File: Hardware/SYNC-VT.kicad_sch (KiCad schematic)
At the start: 0 parts

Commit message: 11/17 progress update
finished the board, now just need to add the peripheral
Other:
- added sheet WiFi_BLE (WiFi_BLE.kicad_sch)
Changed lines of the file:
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@@
+	)
+	(sheet
+		(at 228.6 50.8)
+		(size 25.4 25.4)
+		(fields_autoplaced yes)
+		(stroke
+			(width 0.1524)
+			(type solid)
+		)
+		(fill
+			(color 0 0 0 0.0000)
+		)
+		(property "Sheetname" "WiFi_BLE"
+			(at 228.6 50.0884 0)
+			(effects
+				(font
+					(size 1.27 1.27)
+				)
+				(justify left bottom)
+			)
+		)
+		(property "Sheetfile" "WiFi_BLE.kicad_sch"
+			(at 228.6 76.7846 0)
+			(effects
+				(font
+					(size 1.27 1.27)
+				)
+				(justify left top)
+			)
+		)
+		(instances
+			(project "SYNC-VT"
+				(path "/8b98976c-b0e2-4979-aa9a-b6389ce6c189"
+					(page "8")
+				)
+			)
+		)
 	)
 	(sheet

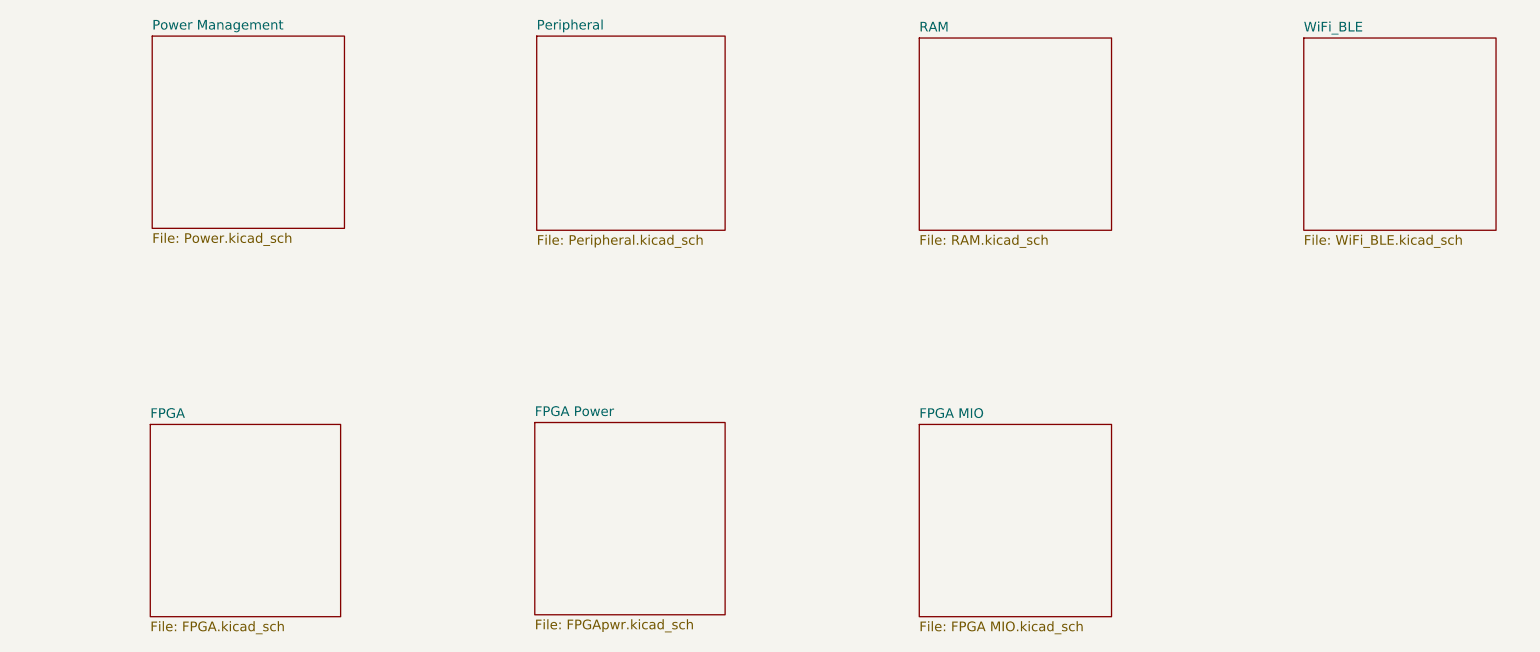
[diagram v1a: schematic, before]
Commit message: 11/19 update
add new header for jtag and fixed a couple of small things
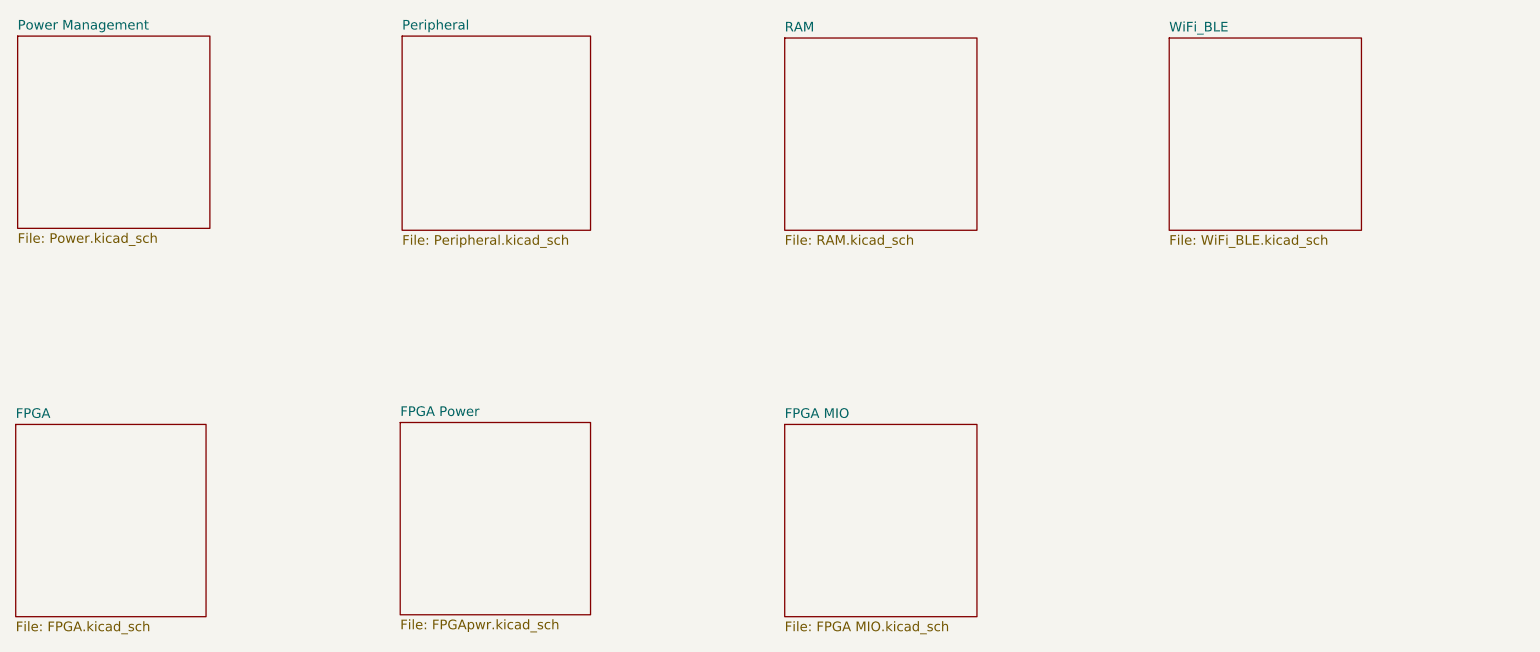
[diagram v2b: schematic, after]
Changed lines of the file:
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@@
 	(paper "A4")
 	(sheet
-		(at 177.8 101.854)
+		(at 160.02 101.854)
 		(size 25.4 25.4)
 		(fields_autoplaced yes)
@@
 		)
 		(property "Sheetname" "FPGA MIO"
-			(at 177.8 101.1424 0)
+			(at 160.02 101.1424 0)
 			(effects
 				(font
@@
 		)
 		(property "Sheetfile" "FPGA MIO.kicad_sch"
-			(at 177.8 127.8386 0)
+			(at 160.02 127.8386 0)
 			(effects
 				(font
@@
 	)
 	(sheet
-		(at 76.454 50.546)
+		(at 58.674 50.546)
 		(size 25.4 25.4)
 		(fields_autoplaced yes)
@@
 		)
 		(property "Sheetname" "Power Management"
-			(at 76.454 49.8344 0)
+			(at 58.674 49.8344 0)
 			(effects
 				(font
@@
 		)
 		(property "Sheetfile" "Power.kicad_sch"
-			(at 76.454 76.5306 0)
+			(at 58.674 76.5306 0)
 			(effects
 				(font
@@
 	)
 	(sheet
-		(at 177.8 50.8)
+		(at 160.02 50.8)
 		(size 25.4 25.4)
 		(fields_autoplaced yes)
@@
 		)
 		(property "Sheetname" "RAM"
-			(at 177.8 50.0884 0)
+			(at 160.02 50.0884 0)
 			(effects
 				(font
@@
 		)
 		(property "Sheetfile" "RAM.kicad_sch"
-			(at 177.8 76.7846 0)
+			(at 160.02 76.7846 0)
 			(effects
 				(font
@@
 	)
 	(sheet
-		(at 228.6 50.8)
+		(at 210.82 50.8)
 		(size 25.4 25.4)
 		(fields_autoplaced yes)
@@
 		)
 		(property "Sheetname" "WiFi_BLE"
-			(at 228.6 50.0884 0)
+			(at 210.82 50.0884 0)
 			(effects
 				(font
@@
 		)
 		(property "Sheetfile" "WiFi_BLE.kicad_sch"
-			(at 228.6 76.7846 0)
+			(at 210.82 76.7846 0)
 			(effects
 				(font
@@
 	)
 	(sheet
-		(at 76.2 101.854)
+		(at 58.42 101.854)
 		(size 25.146 25.4)
 		(fields_autoplaced yes)
@@
 		)
 		(property "Sheetname" "FPGA"
-			(at 76.2 101.1424 0)
+			(at 58.42 101.1424 0)
 			(effects
 				(font
@@
 		)
 		(property "Sheetfile" "FPGA.kicad_sch"
-			(at 76.2 127.8386 0)
+			(at 58.42 127.8386 0)
 			(effects
 				(font
@@
 	)
 	(sheet
-		(at 127 101.6)
+		(at 109.22 101.6)
 		(size 25.146 25.4)
 		(fields_autoplaced yes)
@@
 		)
 		(property "Sheetname" "FPGA Power"
-			(at 127 100.8884 0)
+			(at 109.22 100.8884 0)
 			(effects
 				(font
@@
 		)
 		(property "Sheetfile" "FPGApwr.kicad_sch"
-			(at 127 127.5846 0)
+			(at 109.22 127.5846 0)
 			(effects
 				(font
@@
 	)
 	(sheet
-		(at 127.254 50.546)
+		(at 109.474 50.546)
 		(size 24.892 25.654)
 		(fields_autoplaced yes)
@@
 		)
 		(property "Sheetname" "Peripheral"
-			(at 127.254 49.8344 0)
+			(at 109.474 49.8344 0)
 			(effects
 				(font
@@
 		)
 		(property "Sheetfile" "Peripheral.kicad_sch"
-			(at 127.254 76.7846 0)
-			(effects
-				(font
+			(at 109.474 76.7846 0)
+			(effects
+				(font
